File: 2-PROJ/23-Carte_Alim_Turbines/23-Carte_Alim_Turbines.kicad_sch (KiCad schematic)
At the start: 18 parts, among them J1 Conn_01x03, J2 Conn_01x03, J3 Conn_01x03, J4 690367280676, J5 690367280676, Q1 2N7002, Q2 SUM110P06-08L, U1 ACPL-214-500E, U2 ACPL-214-500E

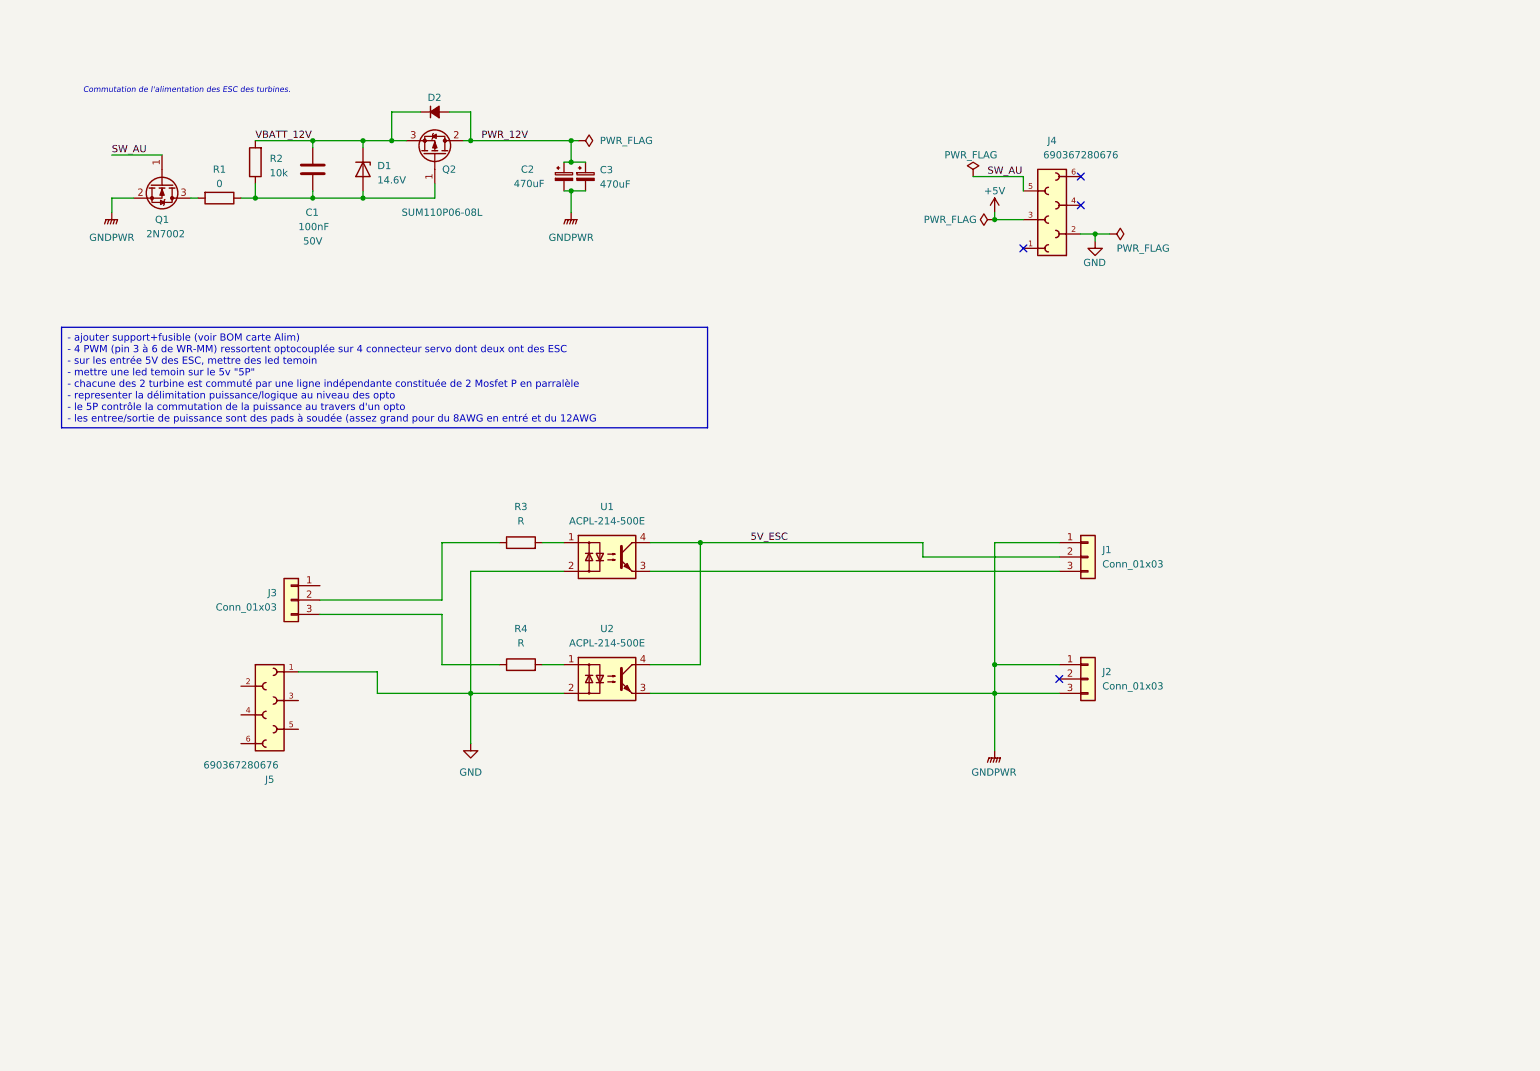
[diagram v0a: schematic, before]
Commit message: Carte Alim Turbines - Schema et Placement
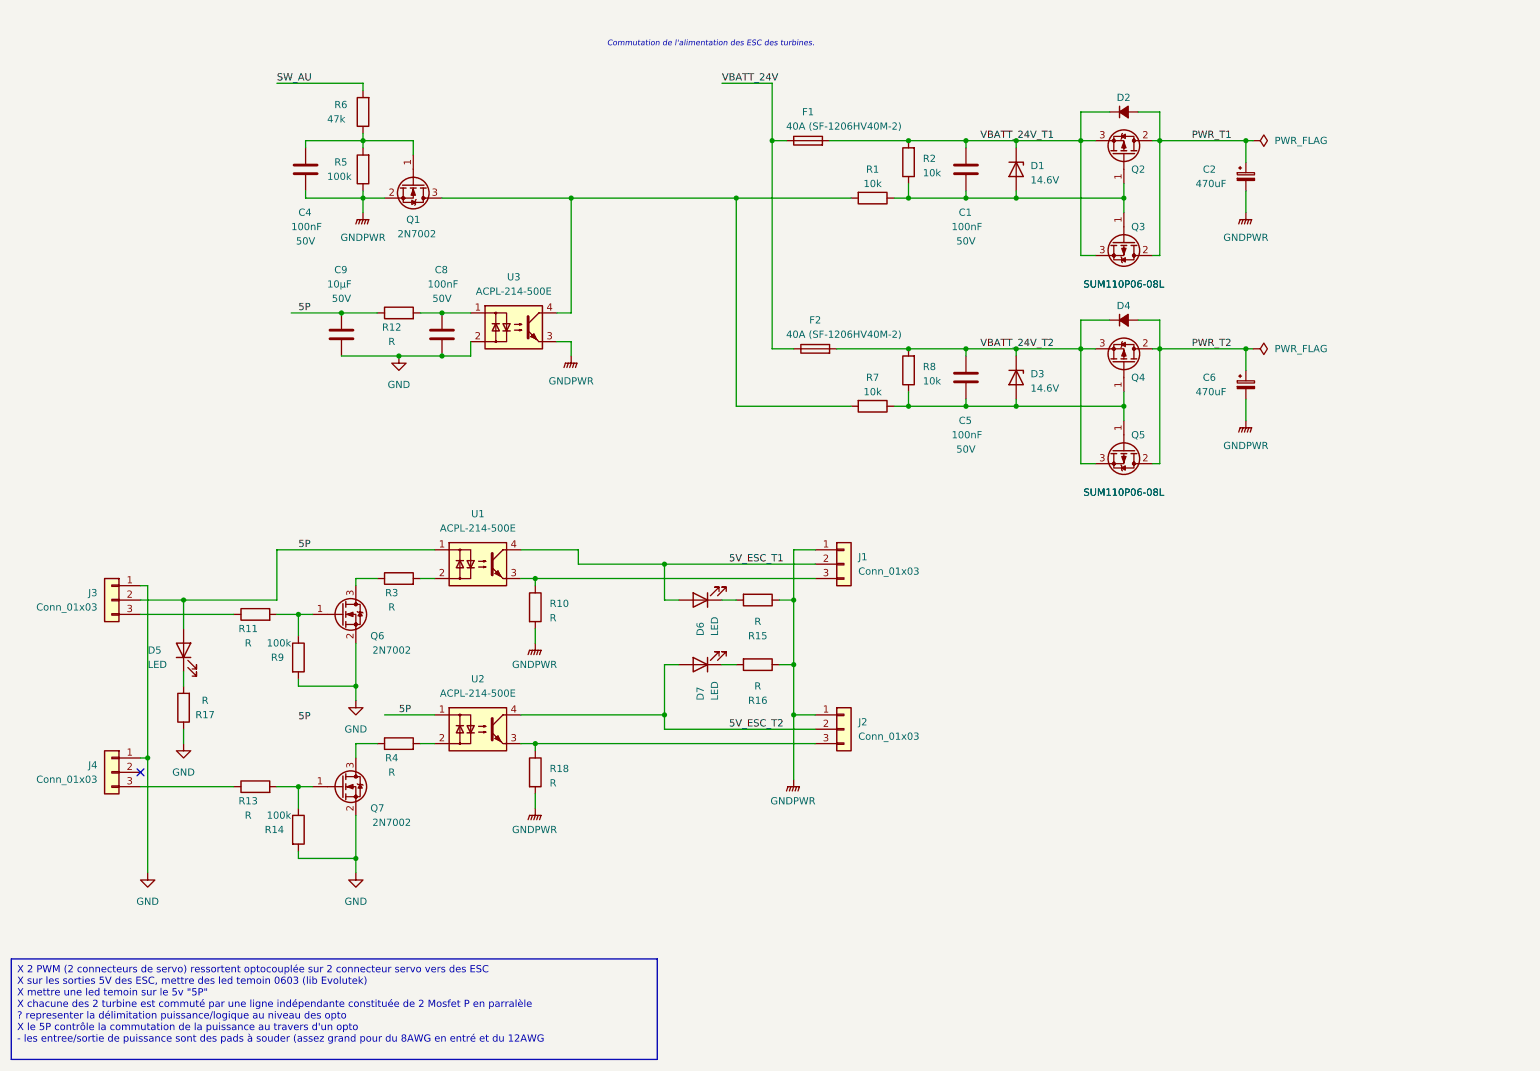
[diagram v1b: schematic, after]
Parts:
- removed C3: 470uF, Capacitor_THT:C_Radial_D8.0mm_H11.5mm_P3.50mm, symbol Device:C_Polarized_Small
- removed J4, J5: 690367280676, ConnectorsEvo:690367280676, symbol ConnectorsEvo:690367280676
- added C4, C5, C8: 100nF, Capacitor_SMD:C_0603_1608Metric, symbol Device:C
- added C6: 470uF, Capacitor_THT:C_Radial_D8.0mm_H11.5mm_P3.50mm, symbol Device:C_Polarized_Small
- added C9: 10µF, Capacitor_SMD:C_0603_1608Metric, symbol Device:C
- added D3: 14.6V, Diode_SMD:D_SOD-323, symbol Device:D_Zener
- added D4: ~, ComponentsEvo:DO-214AB, symbol Device:D_Small_Filled
- added D5, D6, D7: LED, LED_SMD:LED_0603_1608Metric, symbol Device:LED
- added F1, F2: 40A (SF-1206HV40M-2), Fuse:Fuse_1206_3216Metric, symbol Device:Fuse
- added J4: Conn_01x03, Connector_PinHeader_2.54mm:PinHeader_1x03_P2.54mm_Horizontal, symbol Connector_Generic:Conn_01x03
- added Q3, Q4, Q5: SUM110P06-08L, Package_TO_SOT_SMD:TO-263-2, symbol Transistor_FET:QM6015D
- added Q6, Q7: 2N7002, Package_TO_SOT_SMD:SOT-23, symbol Transistor_FET:2N7002
- added R10, R11, R12, R13, R15, R16, R17, R18: R, Resistor_SMD:R_0603_1608Metric, symbol Device:R
- added R14, R5, R9: 100k, Resistor_SMD:R_0603_1608Metric, symbol Device:R
- added R6: 47k, Resistor_SMD:R_0603_1608Metric, symbol Device:R
- added R7, R8: 10k, Resistor_SMD:R_0603_1608Metric, symbol Device:R
- added U3: ACPL-214-500E, Package_SO:SOP-4_4.4x2.6mm_P1.27mm, symbol Isolator:ACPL-214-500E
- J2: footprint (none) -> Connector_PinHeader_2.54mm:PinHeader_1x03_P2.54mm_Horizontal
- R1: value 0 -> 10k
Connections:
- net GND: now also J3.1 (Pin_1), C8.2, C9.2, J4.1 (Pin_1), Q6.2 (S), Q7.2 (S), R14.2, R17.1, R9.2, U3.2; no longer U1.2, U2.2
- net GNDPWR: now also C4.2, C6.2, R10.2, R15.1, R16.1, R18.2, R5.1, U3.3; no longer J2.3 (Pin_3), U2.3
- net SW_AU: now also R6.2; no longer Q1.1 (G)
- net at R4.2: now also U2.2; no longer U2.1
- net at Q1.3 (D), R1.2: now also R7.2, U3.4
- net at R4.1: now also Q7.3 (D); no longer J3.3 (Pin_3)
- net at C1.2, D1.2 (A), Q2.1 (G)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: now also Q3.1 (G)
- net at R3.1: now also Q6.3 (D); no longer J3.2 (Pin_2)
- net at R3.2: now also U1.2; no longer U1.1
- net 5V_ESC_T2: now reaches J2.2 (Pin_2)
- net 5V_ESC_T2: now also U2.4, D7.2 (A)
- net at J1.3 (Pin_3), U1.3: now also R10.1
- net 5V_ESC renamed 5V_ESC_T1
- net 5V_ESC_T1: now also D6.2 (A); no longer U2.4
- net PWR_12V renamed PWR_T1
- net PWR_T1: now also Q3.2 (D)
- net VBATT_12V renamed VBATT_24V_T1
- net VBATT_24V_T1: now also F1.2, Q3.3 (S)
- new net: C4.1, Q1.1 (G), R5.2, R6.1
- new net: J2.3 (Pin_3), R18.1, U2.3
- new net: C5.2, D3.2 (A), Q4.1 (G), Q5.1 (G), R7.1, R8.1
- new net: Q6.1 (G), R11.2, R9.1
- new net: D5.1 (K), R17.2
- new net: Q7.1 (G), R13.2, R14.1
- new net: J4.3 (Pin_3), R13.1
- new net: D7.1 (K), R16.2
- new net: J3.3 (Pin_3), R11.1
- new net: C8.1, R12.2, U3.1
- new net: D6.1 (K), R15.2
- new net 5P: C9.1, D5.2 (A), J3.2 (Pin_2), R12.1, U1.1, U2.1
- new net PWR_T2: C6.1, D4.2 (A), Q4.2 (D), Q5.2 (D)
- new net VBATT_24V: F1.1, F2.1
- new net VBATT_24V_T2: C5.1, D3.1 (K), D4.1 (K), F2.2, Q4.3 (S), Q5.3 (S), R8.2
- no-connect marks 4 -> 1
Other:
- moved on the sheet: C1, C2, D1, D2, J1, J3, Q1, Q2, R1, R2, R3, R4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

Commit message: Work in progress
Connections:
- net 5P: now also U1.2; no longer U1.1
- net at R3.2: now also U1.1; no longer U1.2
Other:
- moved on the sheet: R3
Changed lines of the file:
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@@
     (stroke (width 0) (type default))
   )
-  (wire (pts (xy 60.96 106.68) (xy 88.9 106.68))
+  (wire (pts (xy 210.82 78.74) (xy 210.82 81.28))
     (stroke (width 0) (type default))
   )
-  (wire (pts (xy 210.82 78.74) (xy 210.82 81.28))
+  (wire (pts (xy 86.36 106.68) (xy 88.9 106.68))
     (stroke (width 0) (type default))
   )
@@
     (stroke (width 0) (type default))
   )
-  (wire (pts (xy 78.74 111.76) (xy 74.93 111.76))
+  (wire (pts (xy 78.74 106.68) (xy 74.93 106.68))
     (stroke (width 0) (type default))
   )
@@
     (stroke (width 0) (type default))
   )
+  (wire (pts (xy 60.96 111.76) (xy 88.9 111.76))
+    (stroke (width 0) (type default))
+  )
   (wire (pts (xy 152.4 135.89) (xy 156.21 135.89))
     (stroke (width 0) (type default))
@@
     (stroke (width 0) (type default))
   )
-  (wire (pts (xy 60.96 115.57) (xy 60.96 106.68))
+  (wire (pts (xy 60.96 115.57) (xy 60.96 111.76))
     (stroke (width 0) (type default))
   )
@@
     (stroke (width 0) (type default))
   )
-  (wire (pts (xy 74.93 111.76) (xy 74.93 113.03))
+  (wire (pts (xy 74.93 106.68) (xy 74.93 113.03))
     (stroke (width 0) (type default))
   )
@@
     (stroke (width 0) (type default))
   )
-  (wire (pts (xy 86.36 111.76) (xy 88.9 111.76))
-    (stroke (width 0) (type default))
-  )
   (wire (pts (xy 64.77 118.11) (xy 64.77 121.92))
     (stroke (width 0) (type default))
@@
     (effects (font (size 1.27 1.27)) (justify left bottom))
   )
-  (label "5P" (at 64.77 106.68 0) (fields_autoplaced)
+  (label "5P" (at 52.07 115.57 0) (fields_autoplaced)
     (effects (font (size 1.27 1.27)) (justify left bottom))
   )
@@
     )
   )
-  (symbol (lib_id "Device:R") (at 82.55 111.76 90) (unit 1)
+  (symbol (lib_id "Device:R") (at 82.55 106.68 90) (unit 1)
     (in_bom yes) (on_board yes) (dnp no)
-    (property "Reference" "R3" (at 81.28 114.3 90)
+    (property "Reference" "R3" (at 81.28 109.22 90)
       (effects (font (size 1.27 1.27)))
     )
-    (property "Value" "R" (at 81.28 116.84 90)
+    (property "Value" "R" (at 81.28 111.76 90)
       (effects (font (size 1.27 1.27)))
     )
-    (property "Footprint" "Resistor_SMD:R_0603_1608Metric" (at 82.55 113.538 90)
+    (property "Footprint" "Resistor_SMD:R_0603_1608Metric" (at 82.55 108.458 90)
       (effects (font (size 1.27 1.27)) hide)
     )
-    (property "Datasheet" "~" (at 82.55 111.76 0)
+    (property "Datasheet" "~" (at 82.55 106.68 0)
       (effects (font (size 1.27 1.27)) hide)
     )

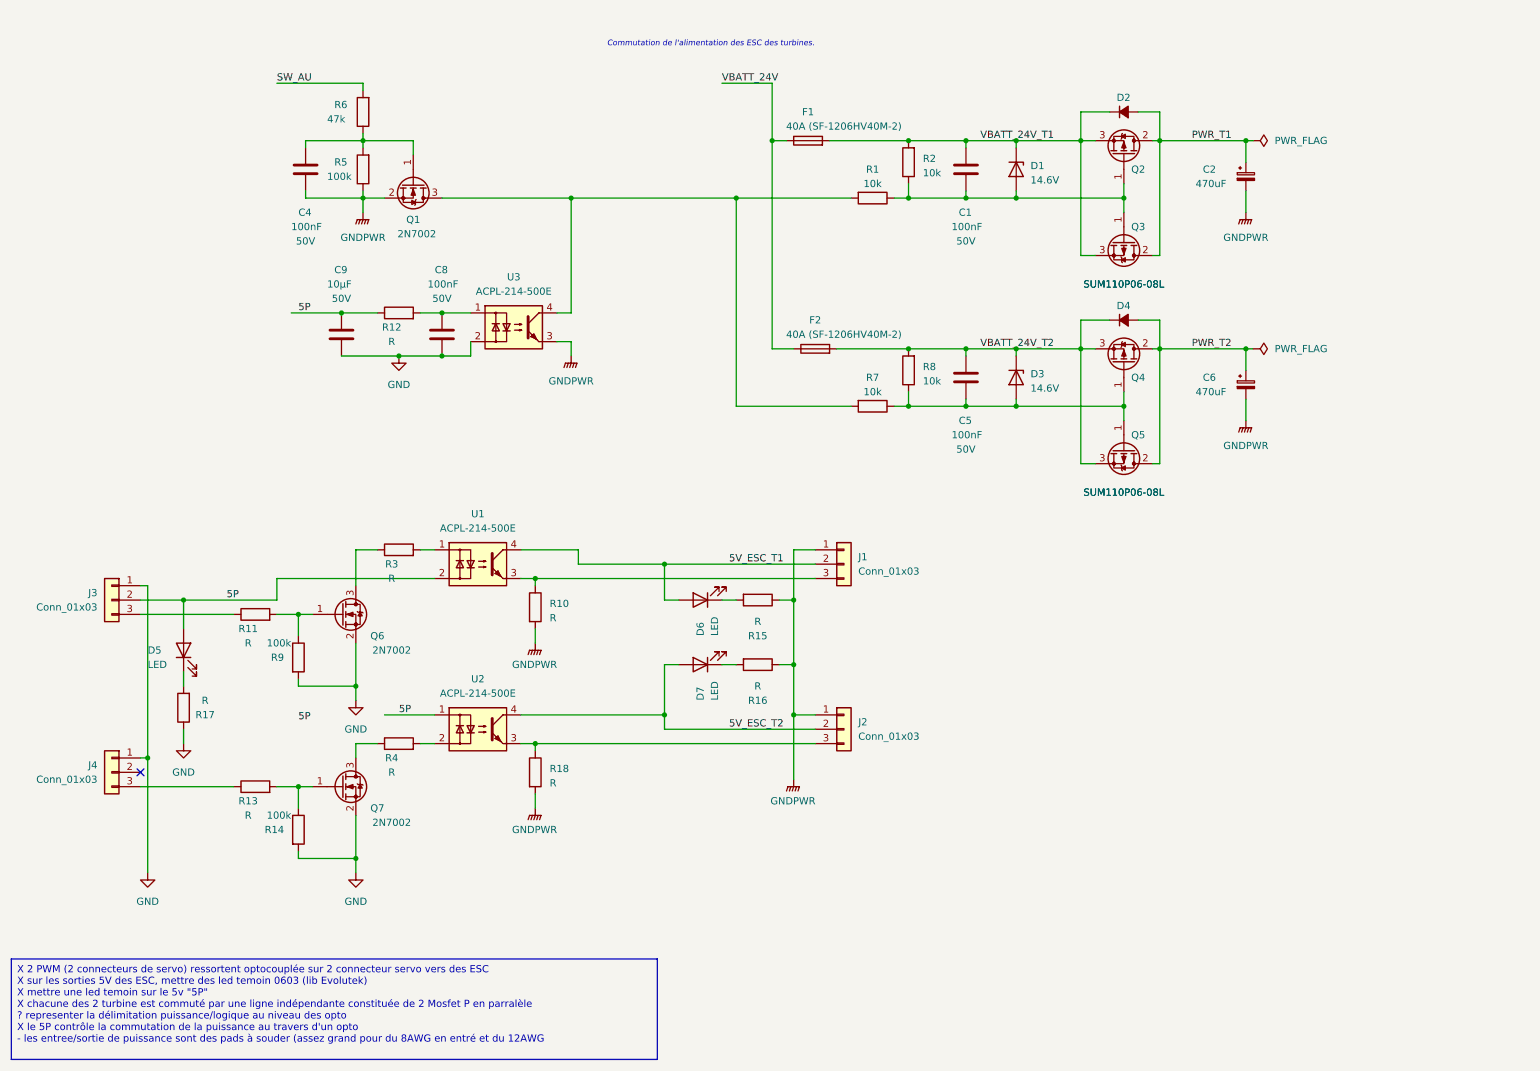
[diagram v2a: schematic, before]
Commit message: fin routage Carte Turbine
et ajout doc Kicad
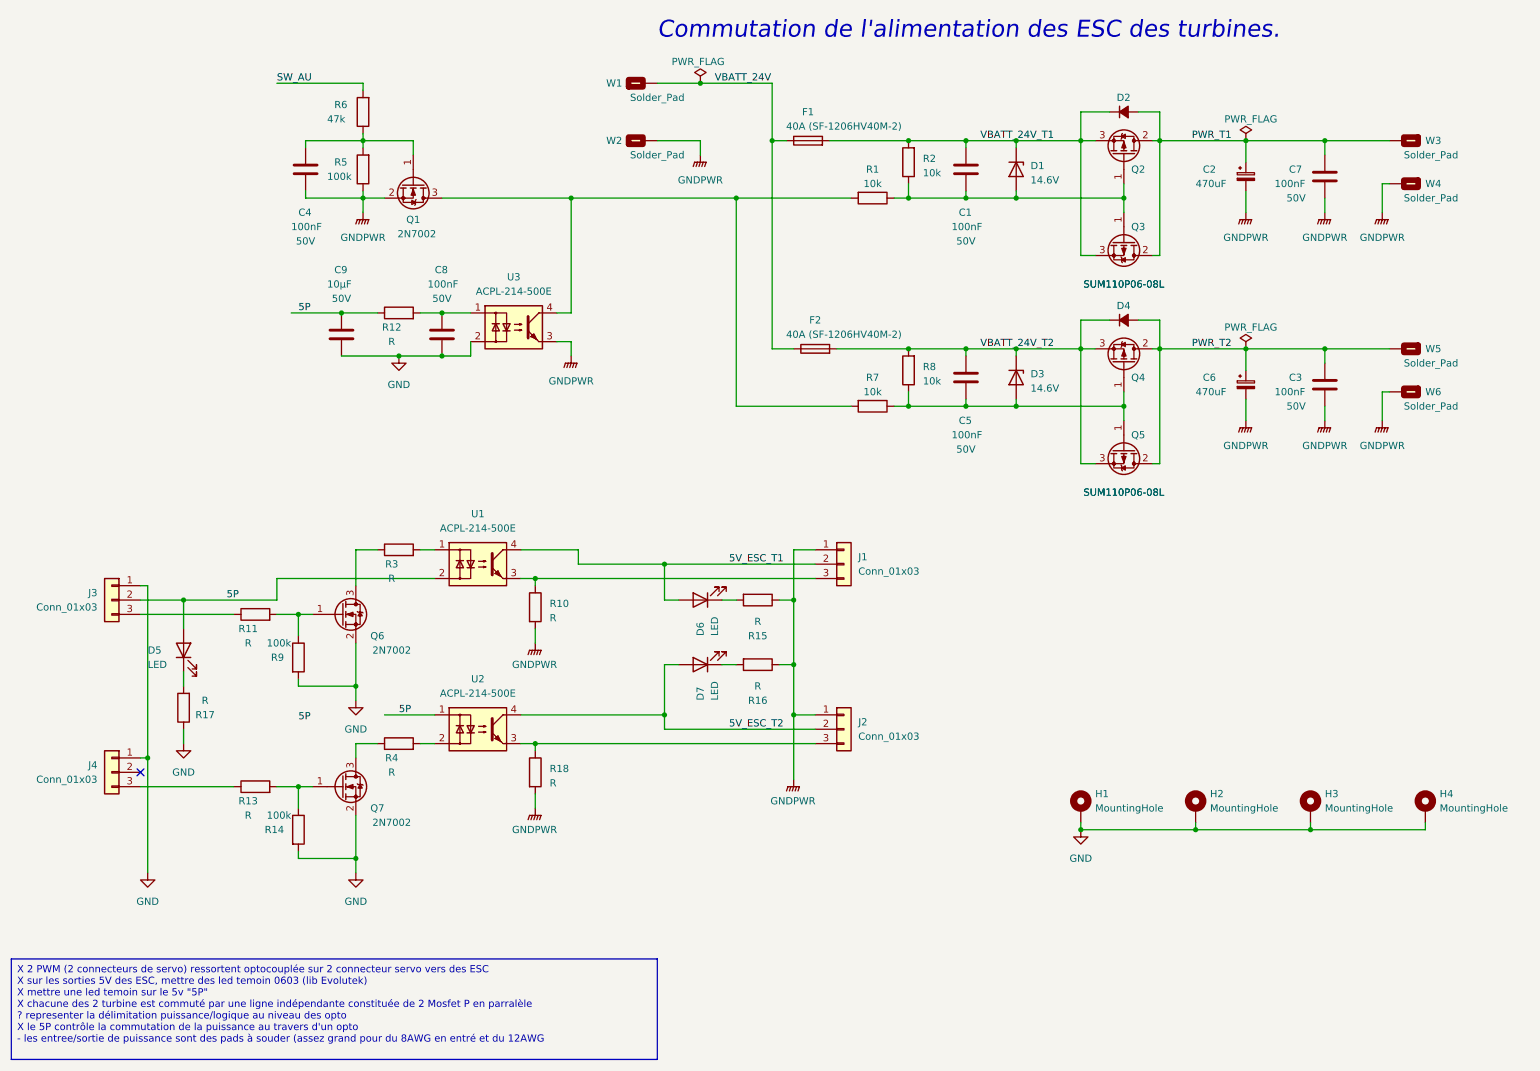
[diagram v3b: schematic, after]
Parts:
- added C3, C7: 100nF, Capacitor_SMD:C_0603_1608Metric, symbol Device:C
- added H1, H2, H3, H4: MountingHole, MountingHole:MountingHole_3.2mm_M3_Pad_Via, symbol Mechanical:MountingHole_Pad
- added W1, W2, W3, W4, W5, W6: Solder_Pad, ConnectorsEvo:WireSolder_Pad_5.0x5.0mm, symbol Mechanical:MountingHole_Pad
- Q2, Q3, Q4, Q5: footprint Package_TO_SOT_SMD:TO-263-2 -> ComponentsEvo:TO-263-2_Goldorak
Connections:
- net GND: now also H1.1, H2.1, H3.1, H4.1
- net GNDPWR: now also C3.2, C7.2, W2.1, W4.1, W6.1
- net PWR_T1: now also C7.1, W3.1
- net PWR_T2: now also C3.1, W5.1
- net VBATT_24V: now also W1.1
